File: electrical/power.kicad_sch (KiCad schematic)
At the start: 30 parts

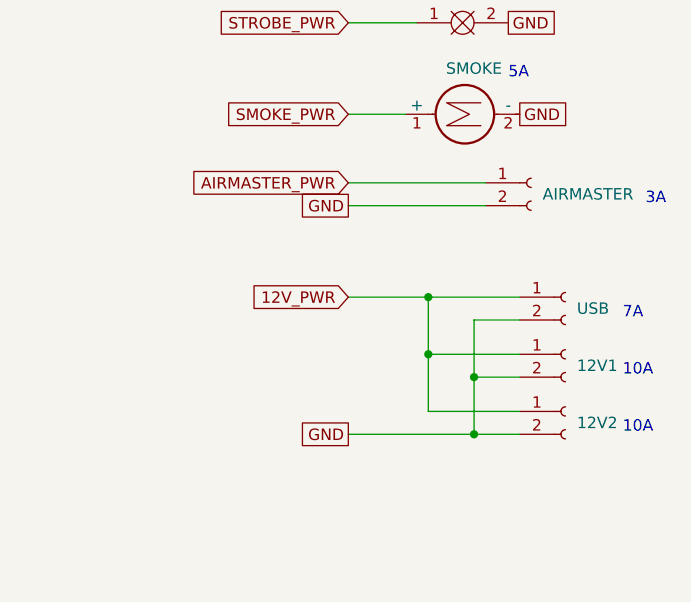
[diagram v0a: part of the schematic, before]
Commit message: Changed so airmaster is a motor and 12V power is a resistor to ahve full connecitons
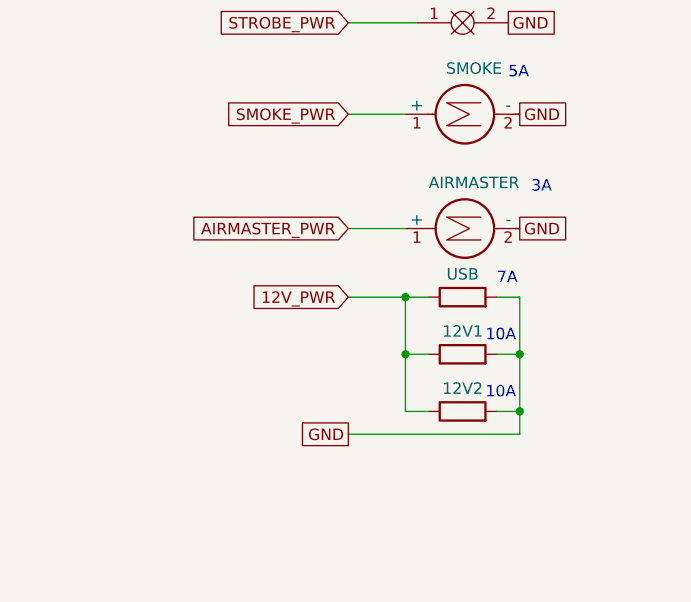
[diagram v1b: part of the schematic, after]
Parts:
- removed 12V1, 12V2, AIRMASTER, USB: Conn_01x02_Socket, symbol Connector:Conn_01x02_Socket
- added 12V1, 12V2, USB: R, symbol Device:R
- added AIRMASTER: Motor_DC, symbol Motor:Motor_DC
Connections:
- net 12V_PWR: now also 12V1.1, 12V2.1, USB.1
- net AIRMASTER_PWR: now also AIRMASTER.1 (+)
- net GND: now also 12V1.2, 12V2.2, AIRMASTER.2 (-), USB.2

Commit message: Added EIS
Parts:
- removed CO_FS: 1, symbol Device:Fuse
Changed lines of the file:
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@@
   (junction (at 173.99 223.52) (diameter 0) (color 0 0 0 0)
-  )
-  (junction (at 173.99 160.02) (diameter 0) (color 0 0 0 0)
   )
   (junction (at 156.21 55.88) (diameter 0) (color 0 0 0 0)
@@
     (stroke (width 0) (type default))
   )
-  (wire (pts (xy 173.99 160.02) (xy 173.99 163.83))
-    (stroke (width 0) (type default))
-  )
   (wire (pts (xy 53.34 68.58) (xy 67.31 68.58))
     (stroke (width 0) (type default))
@@
   )
   (bus (pts (xy 99.06 228.6) (xy 99.06 231.14))
-    (stroke (width 0) (type default))
-  )
-  (wire (pts (xy 173.99 163.83) (xy 176.53 163.83))
     (stroke (width 0) (type default))
   )
@@
   )
   (text "3A" (at 104.14 204.47 0)
-    (effects (font (size 1.27 1.27)) (justify left bottom))
-  )
-  (text "1A" (at 194.31 165.1 0)
     (effects (font (size 1.27 1.27)) (justify left bottom))
   )
@@
   )
   (hierarchical_label "GEA24_PWR" (shape output) (at 81.28 20.32 0) (fields_autoplaced)
-    (effects (font (size 1.27 1.27)) (justify left))
-  )
-  (hierarchical_label "CO_PWR" (shape output) (at 184.15 163.83 0) (fields_autoplaced)
     (effects (font (size 1.27 1.27)) (justify left))
   )
@@
         )
       )
-    )
-  )
-  (symbol (lib_id "Device:Fuse") (at 180.34 163.83 90) (unit 1)
-    (in_bom yes) (on_board yes) (dnp no)
-    (property "Reference" "CO_FS" (at 180.34 160.02 90)
-      (effects (font (size 1.27 1.27)) hide)
-    )
-    (property "Value" "1" (at 180.34 161.29 90)
-      (effects (font (size 1.27 1.27)))
-    )
-    (property "Footprint" "" (at 180.34 165.608 90)
-      (effects (font (size 1.27 1.27)) hide)
-    )
-    (property "Datasheet" "~" (at 180.34 163.83 0)
-      (effects (font (size 1.27 1.27)) hide)
-    )
-    (pin "1")
-    (pin "2")
-    (instances
-      (project "electrical"
-        (path "/e8ec215a-dbe2-4eba-a577-e50a0a128049/2852c073-fbc9-4469-a6bf-ba3e911c7f5a"
-          (reference "CO_FS") (unit 1)
-        )
-      )

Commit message: Added Multifunction
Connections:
- net TRIM_SLATS_PWR renamed TRIM_FLAPS_PWR
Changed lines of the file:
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@@
     (effects (font (size 1.27 1.27)) (justify left))
   )
-  (hierarchical_label "TRIM_SLATS_PWR" (shape output) (at 62.23 152.4 0) (fields_autoplaced)
+  (hierarchical_label "TRIM_FLAPS_PWR" (shape output) (at 62.23 152.4 0) (fields_autoplaced)
     (effects (font (size 1.27 1.27)) (justify left))
   )

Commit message: Updated system overview and added Power 2 to GTX 45R.
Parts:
- added BAK_GTX45R_FS: 3, symbol Device:Fuse
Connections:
- new net GTX45R_BAK_PWR: BAK_GTX45R_FS.2
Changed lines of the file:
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@@
+    (stroke (width 0) (type default))
+  )
+  (bus_entry (at 157.48 93.98) (size 2.54 2.54)
     (stroke (width 0) (type default))
   )
@@
     (stroke (width 0) (type default))
   )
+  (bus (pts (xy 157.48 93.98) (xy 157.48 96.52))
+    (stroke (width 0) (type default))
+  )
   (wire (pts (xy 173.99 153.67) (xy 175.26 153.67))
     (stroke (width 0) (type default))
@@
   )
   (bus (pts (xy 157.48 78.74) (xy 157.48 82.55))
+    (stroke (width 0) (type default))
+  )
+  (wire (pts (xy 160.02 96.52) (xy 161.29 96.52))
     (stroke (width 0) (type default))
   )
@@
   )
   (hierarchical_label "GAD29_BAK_PWR" (shape output) (at 168.91 88.9 0) (fields_autoplaced)
+    (effects (font (size 1.27 1.27)) (justify left))
+  )
+  (hierarchical_label "GTX45R_BAK_PWR" (shape output) (at 168.91 96.52 0) (fields_autoplaced)
     (effects (font (size 1.27 1.27)) (justify left))
   )
@@
         )
       )
+    )
+  )
+  (symbol (lib_id "Device:Fuse") (at 165.1 96.52 90) (unit 1)
+    (in_bom yes) (on_board yes) (dnp no)
+    (property "Reference" "BAK_GTX45R_FS" (at 165.1 92.71 90)
+      (effects (font (size 1.27 1.27)) hide)
+    )
+    (property "Value" "3" (at 165.1 93.98 90)
+      (effects (font (size 1.27 1.27)))
+    )
+    (property "Footprint" "" (at 165.1 98.298 90)
+      (effects (font (size 1.27 1.27)) hide)
+    )
+    (property "Datasheet" "~" (at 165.1 96.52 0)
+      (effects (font (size 1.27 1.27)) hide)
+    )
+    (pin "1")
+    (pin "2")
+    (instances
+      (project "electrical"
+        (path "/e8ec215a-dbe2-4eba-a577-e50a0a128049/2852c073-fbc9-4469-a6bf-ba3e911c7f5a"
+          (reference "BAK_GTX45R_FS") (unit 1)
+        )
+      )
